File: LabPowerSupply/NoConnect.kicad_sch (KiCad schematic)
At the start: 2 parts

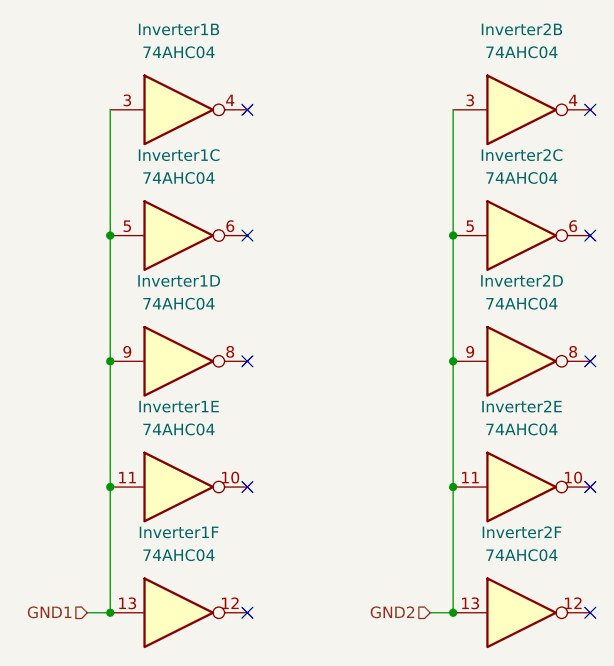
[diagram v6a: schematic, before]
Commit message: Updated Part List
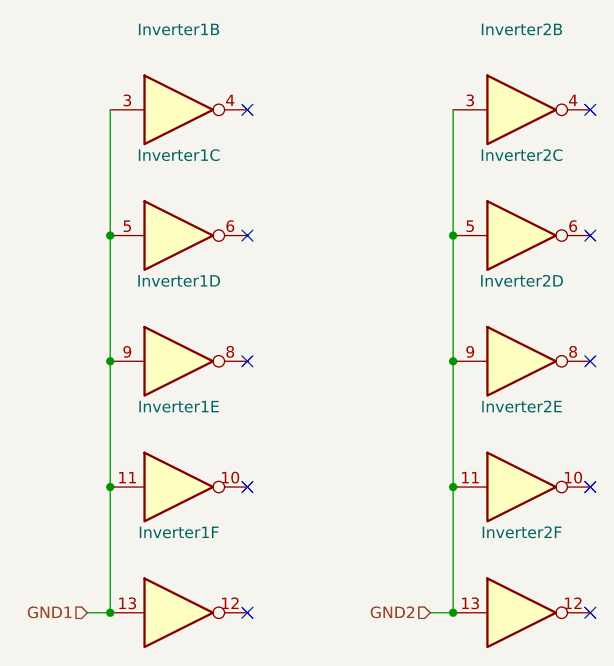
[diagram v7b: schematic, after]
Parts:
- Inverter1, Inverter2: value 74AHC04 -> (none); footprint Package_SO:SSOP-14_5.3x6.2mm_P0.65mm -> (none)
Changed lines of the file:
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@@
     (in_bom yes) (on_board yes) (fields_autoplaced)
     (property "Reference" "Inverter1" (id 0) (at 110.49 97.79 0))
-    (property "Value" "74AHC04" (id 1) (at 110.49 100.33 0))
-    (property "Footprint" "Package_SO:SSOP-14_5.3x6.2mm_P0.65mm" (id 2) (at 110.49 106.68 0)
+    (property "Value" "" (id 1) (at 110.49 100.33 0))
+    (property "Footprint" "" (id 2) (at 110.49 106.68 0)
       (effects (font (size 1.27 1.27)) hide)
     )
@@
     (in_bom yes) (on_board yes) (fields_autoplaced)
     (property "Reference" "Inverter1" (id 0) (at 110.49 111.76 0))
-    (property "Value" "74AHC04" (id 1) (at 110.49 114.3 0))
-    (property "Footprint" "Package_SO:SSOP-14_5.3x6.2mm_P0.65mm" (id 2) (at 110.49 120.65 0)
+    (property "Value" "" (id 1) (at 110.49 114.3 0))
+    (property "Footprint" "" (id 2) (at 110.49 120.65 0)
       (effects (font (size 1.27 1.27)) hide)
     )
@@
     (in_bom yes) (on_board yes) (fields_autoplaced)
     (property "Reference" "Inverter1" (id 0) (at 110.49 69.85 0))
-    (property "Value" "74AHC04" (id 1) (at 110.49 72.39 0))
-    (property "Footprint" "Package_SO:SSOP-14_5.3x6.2mm_P0.65mm" (id 2) (at 110.49 78.74 0)
+    (property "Value" "" (id 1) (at 110.49 72.39 0))
+    (property "Footprint" "" (id 2) (at 110.49 78.74 0)
       (effects (font (size 1.27 1.27)) hide)
     )
@@
     (in_bom yes) (on_board yes) (fields_autoplaced)
     (property "Reference" "Inverter1" (id 0) (at 110.49 55.88 0))
-    (property "Value" "74AHC04" (id 1) (at 110.49 58.42 0))
-    (property "Footprint" "Package_SO:SSOP-14_5.3x6.2mm_P0.65mm" (id 2) (at 110.49 64.77 0)
+    (property "Value" "" (id 1) (at 110.49 58.42 0))
+    (property "Footprint" "" (id 2) (at 110.49 64.77 0)
       (effects (font (size 1.27 1.27)) hide)
     )
@@
     (in_bom yes) (on_board yes) (fields_autoplaced)
     (property "Reference" "Inverter2" (id 0) (at 148.59 83.82 0))
-    (property "Value" "74AHC04" (id 1) (at 148.59 86.36 0))
-    (property "Footprint" "Package_SO:SSOP-14_5.3x6.2mm_P0.65mm" (id 2) (at 148.59 92.71 0)
+    (property "Value" "" (id 1) (at 148.59 86.36 0))
+    (property "Footprint" "" (id 2) (at 148.59 92.71 0)
       (effects (font (size 1.27 1.27)) hide)
     )
@@
     (in_bom yes) (on_board yes) (fields_autoplaced)
     (property "Reference" "Inverter2" (id 0) (at 148.59 55.88 0))
-    (property "Value" "74AHC04" (id 1) (at 148.59 58.42 0))
-    (property "Footprint" "Package_SO:SSOP-14_5.3x6.2mm_P0.65mm" (id 2) (at 148.59 64.77 0)
+    (property "Value" "" (id 1) (at 148.59 58.42 0))
+    (property "Footprint" "" (id 2) (at 148.59 64.77 0)
       (effects (font (size 1.27 1.27)) hide)
     )
@@
     (in_bom yes) (on_board yes) (fields_autoplaced)
     (property "Reference" "Inverter2" (id 0) (at 148.59 97.79 0))
-    (property "Value" "74AHC04" (id 1) (at 148.59 100.33 0))
-    (property "Footprint" "Package_SO:SSOP-14_5.3x6.2mm_P0.65mm" (id 2) (at 148.59 106.68 0)
+    (property "Value" "" (id 1) (at 148.59 100.33 0))
+    (property "Footprint" "" (id 2) (at 148.59 106.68 0)
       (effects (font (size 1.27 1.27)) hide)
     )
@@
     (in_bom yes) (on_board yes) (fields_autoplaced)
     (property "Reference" "Inverter1" (id 0) (at 110.49 83.82 0))
-    (property "Value" "74AHC04" (id 1) (at 110.49 86.36 0))
-    (property "Footprint" "Package_SO:SSOP-14_5.3x6.2mm_P0.65mm" (id 2) (at 110.49 92.71 0)
+    (property "Value" "" (id 1) (at 110.49 86.36 0))
+    (property "Footprint" "" (id 2) (at 110.49 92.71 0)
       (effects (font (size 1.27 1.27)) hide)
     )
@@
     (in_bom yes) (on_board yes) (fields_autoplaced)
     (property "Reference" "Inverter2" (id 0) (at 148.59 111.76 0))
-    (property "Value" "74AHC04" (id 1) (at 148.59 114.3 0))
-    (property "Footprint" "Package_SO:SSOP-14_5.3x6.2mm_P0.65mm" (id 2) (at 148.59 120.65 0)
+    (property "Value" "" (id 1) (at 148.59 114.3 0))
+    (property "Footprint" "" (id 2) (at 148.59 120.65 0)
       (effects (font (size 1.27 1.27)) hide)
     )
@@
     (in_bom yes) (on_board yes) (fields_autoplaced)
     (property "Reference" "Inverter2" (id 0) (at 148.59 69.85 0))
-    (property "Value" "74AHC04" (id 1) (at 148.59 72.39 0))
-    (property "Footprint" "Package_SO:SSOP-14_5.3x6.2mm_P0.65mm" (id 2) (at 148.59 78.74 0)
-      (effects (font (size 1.27 1.27)) hide)
-    )
+    (property "Value" "" (id 1) (at 148.59 72.39 0))
+    (property "Footprint" "" (id 2) (at 148.59 78.74 0)
+      (effects (font (size 1.27 1.27)) hide)
+    )
